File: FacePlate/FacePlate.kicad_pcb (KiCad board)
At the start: 2 copper layers, 131.1 x 44 mm, 27 parts, among them J1 GPIO, J2 Conn_01x05_Male, U3 SX1280, U5 MCP2515-xST, U6 MCP2551-I-SN, Y1 CX532Z-A2B3C5-70-8.0D18

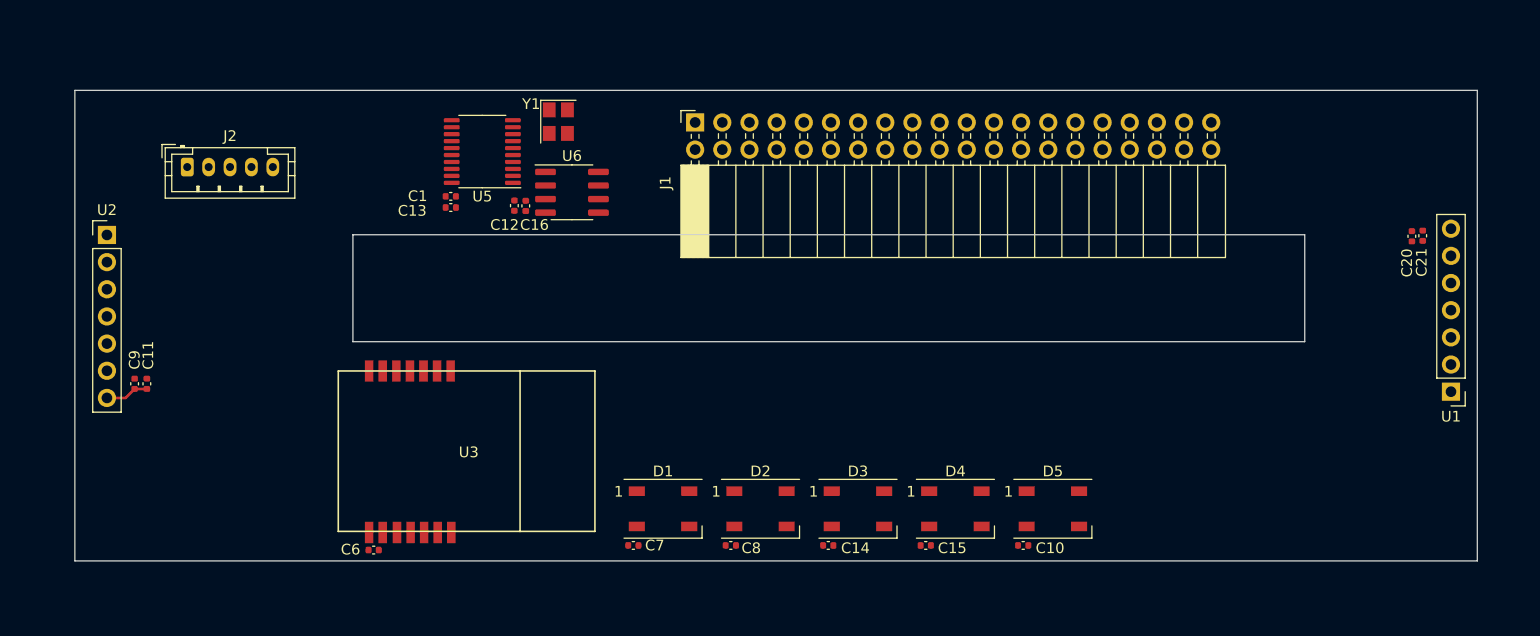
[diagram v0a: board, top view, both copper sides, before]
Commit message: WIP Buck for Faceplate
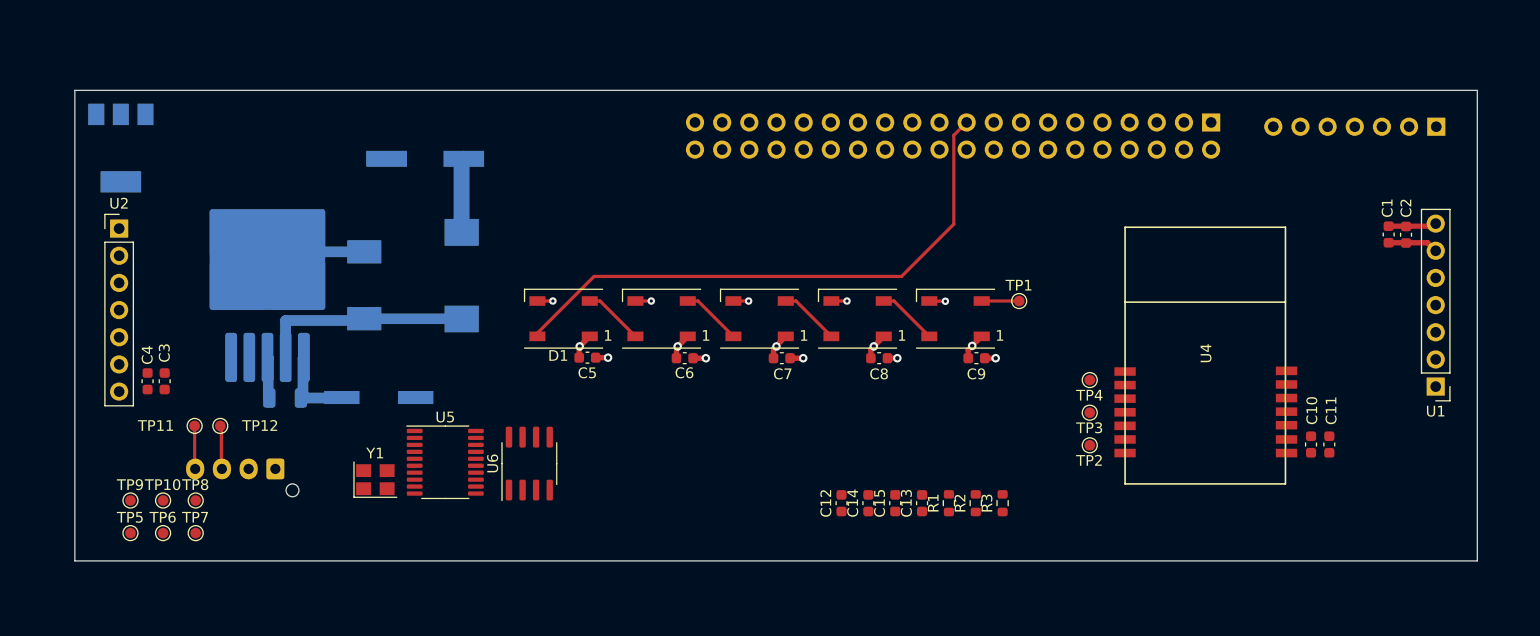
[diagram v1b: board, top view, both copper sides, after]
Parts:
- removed C20, C21: 100n, Capacitor_SMD:C_0402_1005Metric
- removed the J2 at (110.5, 63.2)
- removed the U2 at (103.0, 69.5)
- added C17: EEE-1CA471UP, footprints:CAP_EEE_F_PAN, B.Cu at (132.8, 62.4)
- added C18: 0.47u, Capacitor_SMD:C_1206_3216Metric, B.Cu at (119.7, 84.8)
- added C2: 100n, Capacitor_SMD:C_0603_1608Metric, F.Cu at (224.5, 69.5)
- added C3: 100n, Capacitor_SMD:C_0603_1608Metric, F.Cu at (108.4, 83.2)
- added C4: 100n, Capacitor_SMD:C_0603_1608Metric, F.Cu at (106.8, 83.2)
- added C5: 100n, Capacitor_SMD:C_0603_1608Metric, F.Cu at (147.9, 81.0)
- added CR1: B540C-13-F, footprints:SMC_DIO, B.Cu at (127.1, 74.2)
- added J1: Conn_01x07_Male, Connector_PinSocket_2.54mm:PinSocket_1x07_P2.54mm_Vertical, B.Cu at (227.3, 59.4)
- added J3: Conn_01x04_Pin, Connector_JST:JST_XH_B4B-XH-AM_1x04_P2.50mm_Vertical, B.Cu at (118.8, 91.4)
- added L1: CLF10040T-6R8N-D, footprints:IND_10040_TDK, B.Cu at (136.2, 73.3)
- added R1: 5.1k, Resistor_SMD:R_0603_1608Metric, F.Cu at (181.7, 94.6)
- added R2: 5.1k, Resistor_SMD:R_0603_1608Metric, F.Cu at (184.2, 94.6)
- added R3: 10k, Resistor_SMD:R_0603_1608Metric, F.Cu at (186.8, 94.6)
- added TP1: TestPoint, TestPoint:TestPoint_Pad_D1.0mm, F.Cu at (188.3, 75.7)
- added TP10: TXCAN, TestPoint:TestPoint_Pad_D1.0mm, F.Cu at (108.2, 94.3)
- added TP11: CANH, TestPoint:TestPoint_Pad_D1.0mm, F.Cu at (111.2, 87.4)
- added TP12: CANL, TestPoint:TestPoint_Pad_D1.0mm, F.Cu at (113.6, 87.4)
- added TP2: TestPoint, TestPoint:TestPoint_Pad_D1.0mm, F.Cu at (194.9, 89.2)
- added TP3: TestPoint, TestPoint:TestPoint_Pad_D1.0mm, F.Cu at (194.9, 86.1)
- added TP4: TestPoint, TestPoint:TestPoint_Pad_D1.0mm, F.Cu at (194.9, 83.1)
- added TP5: SI, TestPoint:TestPoint_Pad_D1.0mm, F.Cu at (105.2, 97.4)
- added TP6: SO, TestPoint:TestPoint_Pad_D1.0mm, F.Cu at (108.2, 97.4)
- added TP7: SCK, TestPoint:TestPoint_Pad_D1.0mm, F.Cu at (111.3, 97.4)
- added TP8: CS, TestPoint:TestPoint_Pad_D1.0mm, F.Cu at (111.3, 94.3)
- added TP9: RXCAN, TestPoint:TestPoint_Pad_D1.0mm, F.Cu at (105.2, 94.3)
- added U1: ~, Connector_PinHeader_2.54mm:PinHeader_1x07_P2.54mm_Vertical, F.Cu at (227.2, 83.7)
- added U4: SX1280, SX1280:E28-2G4M12S-SX1280, F.Cu at (205.8, 80.6)
- added U7: AMS1117-3.3, Package_TO_SOT_SMD:SOT-223-3_TabPin2, B.Cu at (104.3, 61.4)
- C1, C10, C11, C6, C7, C8, C9: footprint Capacitor_SMD:C_0402_1005Metric -> Capacitor_SMD:C_0603_1608Metric
- C12, C13: value 100n -> 0.1u; footprint Capacitor_SMD:C_0402_1005Metric -> Capacitor_SMD:C_0603_1608Metric
- C14, C15: value 100n -> 22p; footprint Capacitor_SMD:C_0402_1005Metric -> Capacitor_SMD:C_0603_1608Metric
- C16: value 100n -> 25SVPF100M; footprint Capacitor_SMD:C_0402_1005Metric -> footprints:PCAP_SVP_E7_PAN; moved to B.Cu
- J2: renamed from J1; moved to B.Cu
- U3: value SX1280 -> LM2576S-5; footprint SX1280:E28-2G4M12S-SX1280 -> Package_TO_SOT_SMD:TO-263-5_TabPin3; moved to B.Cu
- Y1: value CX532Z-A2B3C5-70-8.0D18 -> Crystal
- moved U2 125.5 mm to (104.1, 68.9), turned to 0 degrees
- moved C11 110.7 mm to (217.3, 89.1)
- moved C1 87.8 mm to (222.8, 69.5), turned to -90 degrees
- moved C9 78.8 mm to (184.3, 81.0), turned to 0 degrees
- moved C13 52.0 mm to (179.2, 94.6), turned to 90 degrees
- moved J2 48.2 mm to (206.2, 59.0)
- moved C12 41.4 mm to (171.7, 94.6), turned to 90 degrees
- moved Y1 37.6 mm to (128.1, 92.4), turned to 0 degrees
- moved C6 34.2 mm to (157.0, 81.0)
- moved U5 29.3 mm to (134.6, 90.8), turned to 0 degrees
- moved C10 28.5 mm to (215.6, 89.1), turned to 90 degrees
- moved U6 25.7 mm to (142.5, 90.9), turned to 90 degrees
- moved D1 25.6 mm to (145.7, 77.3), turned to 180 degrees
- moved U3 25.0 mm to (118.0, 73.3), turned to 90 degrees
- moved C16 22.6 mm to (128.4, 84.7), turned to 0 degrees
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- renumbered D2 to D1, D1 to D2, U1 to U2
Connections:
- C14 pad 1: +3.3V -> Net-(U5-OSC2)
- C15 pad 1: +3.3V -> Net-(U5-OSC1)
- C16 pad 1: +3.3V -> VDD
- D5 pad 2: /PIXEL_OFFBOARD -> Net-(D5-DOUT)
- J2 pad 13: /SPI6_NSS -> /GPIO_27
- U3 pad 1: +3V3 -> VDD
- U3 pad 2: GND -> /LM_OUT
- U3 pad 3: /SPI6_MISO -> GND
- U3 pad 4: /SPI6_MOSI -> +5V
- U3 pad 5: /SPI6_SCK -> GND
- Y1 pad 1: Net-(U5-OSC1) -> Net-(U5-OSC2)
- Y1 pad 2: Net-(U5-OSC2) -> Net-(U5-OSC1)
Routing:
- net /GPIO[10]/SPI0.MOSI: track 0.00 -> 53.5 mm
- net GND: track 0.00 -> 28.8 mm, vias 0 -> 10
- net /LM_OUT: track 0.00 -> 20.0 mm
- net +3.3V: track 4.08 -> 17.1 mm, vias 0 -> 5
- net VDD: track 0.00 -> 7.76 mm
- net +5V: track 0.00 -> 6.96 mm
- net Net-(D4-DOUT): track 0.00 -> 5.63 mm
- net Net-(D3-DOUT): track 0.00 -> 5.63 mm
- net Net-(D2-DOUT): track 0.00 -> 5.63 mm
- net Net-(D1-DOUT): track 0.00 -> 5.63 mm
- net /CAN/CAN_L: track 0.00 -> 4.36 mm
- net /CAN/CAN_H: track 0.00 -> 4.22 mm
- net Net-(D5-DOUT): track 0.00 -> 3.64 mm
- added copper zone on In2.Cu, net +3.3V
- added copper zone on In1.Cu, net GND
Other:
- outline, holes or cut-outs redrawn
- copper layers 2 -> 4

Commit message: finalize connections
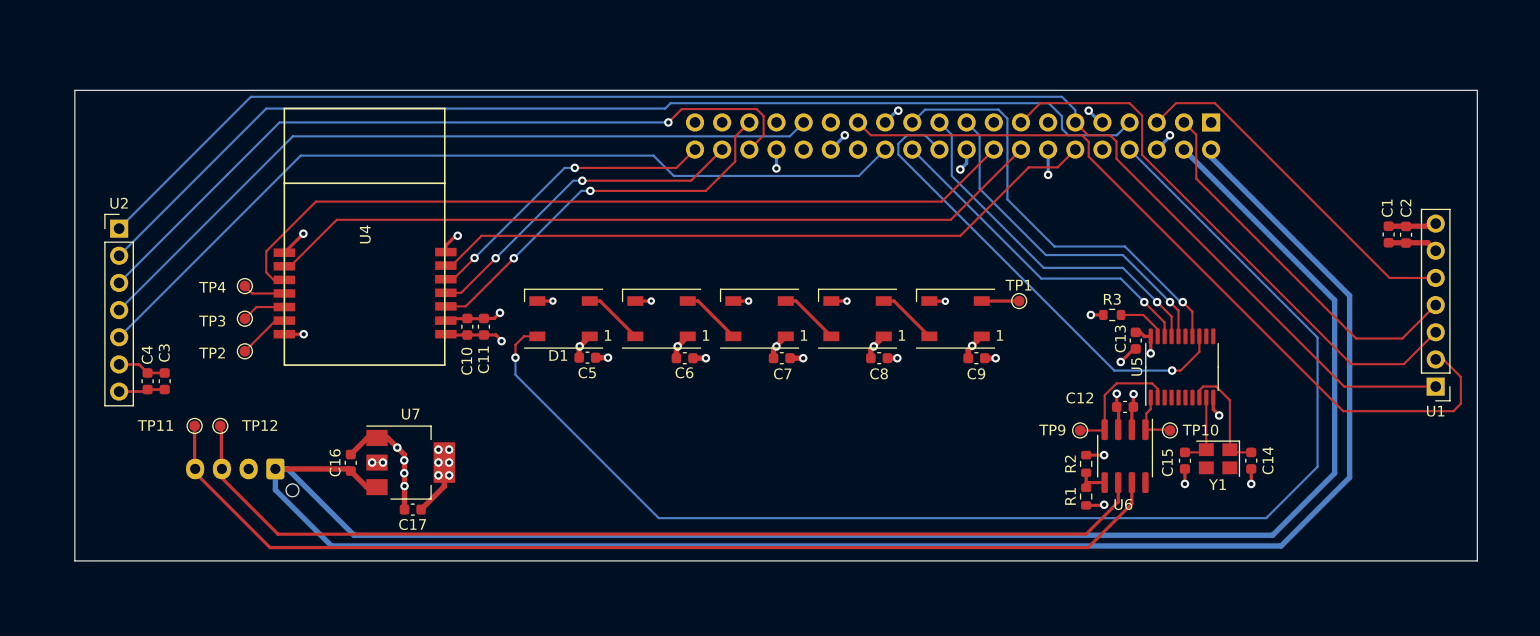
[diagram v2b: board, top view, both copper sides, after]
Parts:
- removed C18: 0.47u, Capacitor_SMD:C_1206_3216Metric
- removed CR1: B540C-13-F, footprints:SMC_DIO
- removed J1: Conn_01x07_Male, Connector_PinSocket_2.54mm:PinSocket_1x07_P2.54mm_Vertical
- removed L1: CLF10040T-6R8N-D, footprints:IND_10040_TDK
- removed TP5: SI, TestPoint:TestPoint_Pad_D1.0mm
- removed TP6: SO, TestPoint:TestPoint_Pad_D1.0mm
- removed TP7: SCK, TestPoint:TestPoint_Pad_D1.0mm
- removed TP8: CS, TestPoint:TestPoint_Pad_D1.0mm
- removed U3: LM2576S-5, Package_TO_SOT_SMD:TO-263-5_TabPin3
- C16: value 25SVPF100M -> 10u; footprint footprints:PCAP_SVP_E7_PAN -> Capacitor_SMD:C_0603_1608Metric; moved to F.Cu
- C17: value EEE-1CA471UP -> 22u; footprint footprints:CAP_EEE_F_PAN -> Capacitor_SMD:C_0603_1608Metric; moved to F.Cu
- U7: moved to F.Cu
- moved TP10 94.4 mm to (202.4, 87.8)
- moved TP9 89.0 mm to (194.0, 87.8)
- moved C11 79.8 mm to (138.2, 78.1)
- moved C10 79.7 mm to (136.7, 78.1)
- moved TP2 79.5 mm to (115.9, 80.4)
- moved TP3 79.5 mm to (115.9, 77.3)
- moved TP4 79.5 mm to (115.9, 74.3)
- moved U4 79.4 mm to (127.2, 69.5)
- moved Y1 78.8 mm to (206.9, 90.5), turned to 180 degrees
- moved U5 69.5 mm to (203.5, 81.9), turned to 90 degrees
- moved U6 55.7 mm to (198.2, 90.2), turned to -90 degrees
- moved U7 40.0 mm to (131.4, 90.8), turned to 0 degrees
- moved C14 36.0 mm to (210.0, 90.6), turned to -90 degrees
- moved C17 32.8 mm to (131.6, 95.2)
- moved C12 28.0 mm to (198.2, 85.6), turned to 0 degrees
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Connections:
- C16 pad 1: VDD -> +5V
- C17 pad 1: +5V -> +3.3V
- D1 pad 4: /GPIO[10]/SPI0.MOSI -> /SPI5_MOSI
- J2 pad 1: +3.3V -> unconnected-(J2-Pin_1-Pad1)
- J2 pad 17: +3.3V -> unconnected-(J2-Pin_17-Pad17)
- J2 pad 19: /GPIO[10]/SPI0.MOSI -> /SPI0_MOSI
- J2 pad 21: /GPIO[9]/SPI0.MISO -> /SPI0_MISO
- J2 pad 23: /GPIO[11]/SPI0.SCLK -> /SPI0_SCLK
- J2 pad 24: /GPIO[8]/SPI0.CE0 -> /SPI0_NSS
- J3 pad 1: VDD -> +5V
- U1 pad 3: /SPI3_MISO -> /GPIO[22]
- U2 pad 3: /SPI4_MISO -> /GPIO[16]
- U5 pad 14: /SPI5_SCLK -> /SPI0_SCLK
- U5 pad 16: /SPI5_MOSI -> /SPI0_MOSI
- U5 pad 17: /SPI5_MISO -> /SPI0_MISO
- U5 pad 18: /SPI5_NSS -> /SPI0_NSS
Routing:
- net +5V: track 6.96 -> 293.6 mm
- net /GPIO[17]: track 0.00 -> 141.1 mm
- net /SPI5_MOSI: track 0.00 -> 124.7 mm, vias 0 -> 1
- net /SPI4_NSS: track 0.00 -> 102.8 mm
- net /CAN/CAN_H: track 4.22 -> 98.7 mm
- net /CAN/CAN_L: track 4.36 -> 94.3 mm
- net /SPI4_CLK: track 0.00 -> 80.5 mm
- net /GPIO[24]: track 0.00 -> 75.9 mm
- net /SPI3_NSS: track 0.00 -> 74.2 mm
- net /GPIO[23]: track 0.00 -> 73.4 mm
- net /SPI4_MOSI: track 0.00 -> 71.3 mm
- net /GPIO[16]: track 0.00 -> 71.0 mm, vias 0 -> 1
- net /SPI6_NSS: track 0.00 -> 63.4 mm
- net /GPIO[10]/SPI0.MOSI: track 53.5 -> 0.00 mm
- net /GPIO[22]: track 0.00 -> 53.0 mm
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
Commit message: Finalize faceplate
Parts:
- removed C14, C15: 22p, Capacitor_SMD:C_0603_1608Metric
- removed Y1: Crystal, Crystal:Crystal_SMD_3225-4Pin_3.2x2.5mm
- added C18: 22p, Capacitor_SMD:C_0603_1608Metric, F.Cu at (210.6, 80.4)
- added C19: 22p, Capacitor_SMD:C_0603_1608Metric, F.Cu at (210.6, 88.4)
- added H1: MountingHole, MountingHole:MountingHole_2.7mm_M2.5, F.Cu at (103.3, 96.8)
- added H2: MountingHole, MountingHole:MountingHole_2.7mm_M2.5, F.Cu at (103.3, 59.2)
- added H3: MountingHole, MountingHole:MountingHole_2.7mm_M2.5, F.Cu at (227.9, 59.3)
- added H4: MountingHole, MountingHole:MountingHole_2.7mm_M2.5, F.Cu at (227.9, 96.7)
- added H5: MountingHole, MountingHole:MountingHole_2.7mm_M2.5, F.Cu at (147.9, 75.3)
- added H6: MountingHole, MountingHole:MountingHole_2.7mm_M2.5, F.Cu at (147.9, 88.3)
- added H7: MountingHole, MountingHole:MountingHole_2.7mm_M2.5, F.Cu at (184.7, 75.3)
- added H8: MountingHole, MountingHole:MountingHole_2.7mm_M2.5, F.Cu at (184.7, 88.3)
- added Y2: ABM3-8.000MHZ-D2Y-T, footprints:XTAL_ABM3-8.000MHZ-D2Y-T_ABR, F.Cu at (209.6, 84.4)
- moved C9 11.5 mm to (173.7, 85.6), turned to 180 degrees
- moved D1 7.34 mm to (151.5, 81.8)
- moved C8 7.29 mm to (180.9, 85.6), turned to 180 degrees
- moved D2 6.11 mm to (159.0, 81.8)
- moved C5 5.81 mm to (151.6, 85.5), turned to 180 degrees
- moved D3 5.11 mm to (166.4, 81.8)
- moved C6 4.92 mm to (159.0, 85.5), turned to 180 degrees
- moved D5 4.58 mm to (181.5, 81.8)
- moved D4 4.57 mm to (174.0, 81.8)
- moved C7 4.46 mm to (166.3, 85.5), turned to 180 degrees
- moved TP1 4.10 mm to (188.4, 79.8)
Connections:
- U5 pad 8: Net-(U5-OSC2) -> /CAN/OSC2
- U5 pad 9: Net-(U5-OSC1) -> /CAN/OSC1
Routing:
- net GND: track 70.9 -> 87.7 mm, vias 31 -> 26
- net Net-(U5-OSC2): track 10.9 -> 0.00 mm
- net /CAN/OSC2: track 0.00 -> 10.4 mm
- net /CAN/OSC1: track 0.00 -> 9.22 mm
- net Net-(U5-OSC1): track 7.33 -> 0.00 mm
- net +3.3V: track 43.3 -> 46.4 mm
- net /SPI5_MOSI: track 124.7 -> 126.9 mm
- net Net-(D2-DOUT): track 5.63 -> 4.36 mm
- net Net-(D4-DOUT): track 5.63 -> 4.38 mm
- net Net-(D1-DOUT): track 5.63 -> 4.38 mm
- net Net-(D3-DOUT): track 5.63 -> 4.40 mm
- net Net-(D5-DOUT): track 3.64 -> 4.62 mm
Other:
- board text added: "The Bots Faceplate Designed by Akhil V"

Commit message: Fix stuff up
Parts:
- moved C11 4.41 mm to (136.3, 82.0), turned to 0 degrees
- moved C10 2.43 mm to (136.3, 80.5), turned to 0 degrees
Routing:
- net GND: track 87.7 -> 19.1 mm, vias 26 -> 2
- net +5V: track 293.6 -> 298.2 mm
- net +3.3V: track 46.4 -> 47.4 mm, vias 18 -> 21
- net /GPIO[24]: track 75.9 -> 76.7 mm
- net /SPI6_NSS: track 63.4 -> 63.9 mm
- added copper zone on F.Cu, net GND
